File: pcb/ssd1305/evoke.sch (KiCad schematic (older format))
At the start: 17 parts, among them U1 STM32F103C8Tx

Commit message: Fix bug with pins being wrong on connector, and add USART header
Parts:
- added J1: Conn_01x03_Male, Connector_PinHeader_2.54mm:PinHeader_1x03_P2.54mm_Vertical, symbol Connector:Conn_01x03_Male
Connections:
- net +3V3: now also LCD_CONN1.21 (Pin_21); no longer LCD_CONN1.20 (Pin_20)
- net GND: now also LCD_CONN1.20 (Pin_20), J1.3 (Pin_3); no longer LCD_CONN1.21 (Pin_21)
- net USART1_TX: now reaches U1.30 (PA9)
- net USART1_TX: now also J1.1 (Pin_1)
- net USART1_RX: now reaches U1.31 (PA10)
- net USART1_RX: now also J1.2 (Pin_2)
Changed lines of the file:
@@
-	1    0    0    -1
-$EndComp
-$Comp
-L evoke-rescue:GND-power #PWR0102
-U 1 1 5EAB6769
-P 3600 5250
-F 0 "#PWR0102" H 3600 5000 50  0001 C CNN
-F 1 "GND" H 3605 5077 50  0000 C CNN
-F 2 "" H 3600 5250 50  0001 C CNN
-F 3 "" H 3600 5250 50  0001 C CNN
-	1    3600 5250
 	1    0    0    -1
 $EndComp
@@
 L evoke-rescue:GND-power #PWR0103
 U 1 1 5EABAA37
-P 3400 5250
-F 0 "#PWR0103" H 3400 5000 50  0001 C CNN
-F 1 "GND" H 3405 5077 50  0000 C CNN
-F 2 "" H 3400 5250 50  0001 C CNN
-F 3 "" H 3400 5250 50  0001 C CNN
-	1    3400 5250
-	1    0    0    -1
-$EndComp
-$Comp
-L evoke-rescue:+3V3-power #PWR0104
-U 1 1 5EABC207
 P 3500 5250
-F 0 "#PWR0104" H 3500 5100 50  0001 C CNN
-F 1 "+3V3" H 3515 5423 50  0000 C CNN
+F 0 "#PWR0103" H 3500 5000 50  0001 C CNN
+F 1 "GND" H 3505 5077 50  0000 C CNN
 F 2 "" H 3500 5250 50  0001 C CNN
 F 3 "" H 3500 5250 50  0001 C CNN
@@
 Wire Wire Line
 	9850 2150 10000 2150
+Wire Wire Line
+	3400 5250 3500 5250
+Connection ~ 3500 5250
+Wire Wire Line
+	4200 5250 3600 5250
+Connection ~ 4200 5250
+Wire Wire Line
+	6350 3600 6550 3600
+Wire Wire Line
+	6350 3700 6550 3700
+Text GLabel 6550 3600 2    50   Input ~ 0
+USART1_TX
+Text GLabel 6550 3700 2    50   Input ~ 0
+USART1_RX
+$Comp
+L Connector:Conn_01x03_Male J1
+U 1 1 5ED86F10
+P 5550 5700
+F 0 "J1" H 5658 5981 50  0000 C CNN
+F 1 "Conn_01x03_Male" H 5658 5890 50  0000 C CNN
+F 2 "Connector_PinHeader_2.54mm:PinHeader_1x03_P2.54mm_Vertical" H 5550 5700 50  0001 C CNN
+F 3 "~" H 5550 5700 50  0001 C CNN
+	1    5550 5700
+	1    0    0    -1
+$EndComp
+Wire Wire Line
+	5750 5600 6050 5600
+Wire Wire Line
+	5750 5700 6050 5700
+Wire Wire Line
+	5750 5800 6050 5800
+$Comp
+L power:GND #PWR0102
+U 1 1 5ED93166
+P 6050 5800
+F 0 "#PWR0102" H 6050 5550 50  0001 C CNN
+F 1 "GND" H 6055 5627 50  0000 C CNN
+F 2 "" H 6050 5800 50  0001 C CNN
+F 3 "" H 6050 5800 50  0001 C CNN
+	1    6050 5800
+	1    0    0    -1
+$EndComp
+Text GLabel 6050 5600 2    50   Input ~ 0
+USART1_TX
+Text GLabel 6050 5700 2    50   Input ~ 0
+USART1_RX
 $EndSCHEMATC

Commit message: Addition of additional components as per jack wan's schematic example
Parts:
- removed C10: 100nF, Capacitor_SMD:C_0805_2012Metric, symbol evoke-rescue:C-Device
- added C10, C12: 100nF, Capacitor_SMD:C_0805_2012Metric, symbol Device:C
- added C11: 10uF, Capacitor_Tantalum_SMD:CP_EIA-3216-18_Kemet-A, symbol Device:CP
- added C13: 4.7uF, Capacitor_Tantalum_SMD:CP_EIA-3216-18_Kemet-A, symbol evoke-rescue:CP-Device
- C1: value 10uF -> 4.7uF; LCSC C7171 -> (none)
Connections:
- net +3V3: now also C12.1, C13.1
- net GND: now also C10.2, C11.2, C12.2, C13.2
- net VCC: now also C10.1, C11.1
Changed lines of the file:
@@
 P 1800 5900
 F 0 "C1" H 1918 5946 50  0000 L CNN
-F 1 "10uF" H 1918 5855 50  0000 L CNN
+F 1 "4.7uF" H 1918 5855 50  0000 L CNN
 F 2 "Capacitor_Tantalum_SMD:CP_EIA-3216-18_Kemet-A" H 1838 5750 50  0001 C CNN
 F 3 "~" H 1800 5900 50  0001 C CNN
-F 4 " C7171" H 1800 5900 50  0001 C CNN "LCSC"
+F 4 " " H 1800 5900 50  0001 C CNN "LCSC"
 	1    1800 5900
 	1    0    0    -1
@@
 	1    0    0    -1
 $EndComp
-$Comp
-L evoke-rescue:C-Device C10
-U 1 1 5EA8CE78
-P 2150 5900
-F 0 "C10" H 2265 5946 50  0000 L CNN
-F 1 "100nF" H 2265 5855 50  0000 L CNN
-F 2 "Capacitor_SMD:C_0805_2012Metric" H 2188 5750 50  0001 C CNN
-F 3 "~" H 2150 5900 50  0001 C CNN
-F 4 "C49678" H 2150 5900 50  0001 C CNN "LCSC"
-	1    2150 5900
-	1    0    0    -1
-$EndComp
-Wire Wire Line
-	2150 6050 1800 6050
-Connection ~ 1800 6050
-Wire Wire Line
-	2150 5750 1800 5750
-Connection ~ 1800 5750
 Wire Wire Line
 	6350 4000 6750 4000
@@
 Text GLabel 6050 5700 2    50   Input ~ 0
 USART1_RX
+$Comp
+L Device:C C10
+U 1 1 5ED7135E
+P 1950 6650
+F 0 "C10" H 1750 6700 50  0000 L CNN
+F 1 "100nF" H 1650 6600 50  0000 L CNN
+F 2 "Capacitor_SMD:C_0805_2012Metric" H 1988 6500 50  0001 C CNN
+F 3 "~" H 1950 6650 50  0001 C CNN
+	1    1950 6650
+	1    0    0    -1
+$EndComp
+$Comp
+L Device:CP C11
+U 1 1 5ED73E93
+P 2250 6650
+F 0 "C11" H 2368 6696 50  0000 L CNN
+F 1 "10uF" H 2368 6605 50  0000 L CNN
+F 2 "Capacitor_Tantalum_SMD:CP_EIA-3216-18_Kemet-A" H 2288 6500 50  0001 C CNN
+F 3 "~" H 2250 6650 50  0001 C CNN
+	1    2250 6650
+	1    0    0    -1
+$EndComp
+Wire Wire Line
+	1950 6800 2100 6800
+Wire Wire Line
+	1950 6500 2100 6500
+$Comp
+L power:GND #PWR0104
+U 1 1 5ED7C439
+P 2100 6800
+F 0 "#PWR0104" H 2100 6550 50  0001 C CNN
+F 1 "GND" H 2105 6627 50  0000 C CNN
+F 2 "" H 2100 6800 50  0001 C CNN
+F 3 "" H 2100 6800 50  0001 C CNN
+	1    2100 6800
+	1    0    0    -1
+$EndComp
+Connection ~ 2100 6800
+Wire Wire Line
+	2100 6800 2250 6800
+Text GLabel 2100 6400 1    50   Input ~ 0
+VCC
+Wire Wire Line
+	2100 6400 2100 6500
+Connection ~ 2100 6500
+Wire Wire Line
+	2100 6500 2250 6500
+$Comp
+L evoke-rescue:CP-Device C13
+U 1 1 5ED88180
+P 3250 6600
+F 0 "C13" H 3368 6646 50  0000 L CNN
+F 1 "4.7uF" H 3368 6555 50  0000 L CNN
+F 2 "Capacitor_Tantalum_SMD:CP_EIA-3216-18_Kemet-A" H 3288 6450 50  0001 C CNN
+F 3 "~" H 3250 6600 50  0001 C CNN
+F 4 " " H 3250 6600 50  0001 C CNN "LCSC"
+	1    3250 6600
+	1    0    0    -1
+$EndComp
+$Comp
+L Device:C C12
+U 1 1 5ED88A1A
+P 3000 6600
+F 0 "C12" H 2800 6650 50  0000 L CNN
+F 1 "100nF" H 2700 6550 50  0000 L CNN
+F 2 "Capacitor_SMD:C_0805_2012Metric" H 3038 6450 50  0001 C CNN
+F 3 "~" H 3000 6600 50  0001 C CNN
+	1    3000 6600
+	1    0    0    -1
+$EndComp
+Wire Wire Line
+	3000 6750 3100 6750
+Wire Wire Line
+	3250 6450 3100 6450
+$Comp
+L evoke-rescue:+3V3-power #PWR0114
+U 1 1 5ED91A37
+P 3100 6450
+F 0 "#PWR0114" H 3100 6300 50  0001 C CNN
+F 1 "+3V3" H 3115 6623 50  0000 C CNN
+F 2 "" H 3100 6450 50  0001 C CNN
+F 3 "" H 3100 6450 50  0001 C CNN
+	1    3100 6450
+	1    0    0    -1
+$EndComp
+Connection ~ 3100 6450
+Wire Wire Line
+	3100 6450 3000 6450
+$Comp
+L power:GND #PWR0115
+U 1 1 5ED921BC
+P 3100 6750
+F 0 "#PWR0115" H 3100 6500 50  0001 C CNN
+F 1 "GND" H 3105 6577 50  0000 C CNN
+F 2 "" H 3100 6750 50  0001 C CNN
+F 3 "" H 3100 6750 50  0001 C CNN
+	1    3100 6750
+	1    0    0    -1
+$EndComp
+Connection ~ 3100 6750
+Wire Wire Line
+	3100 6750 3250 6750
 $EndSCHEMATC

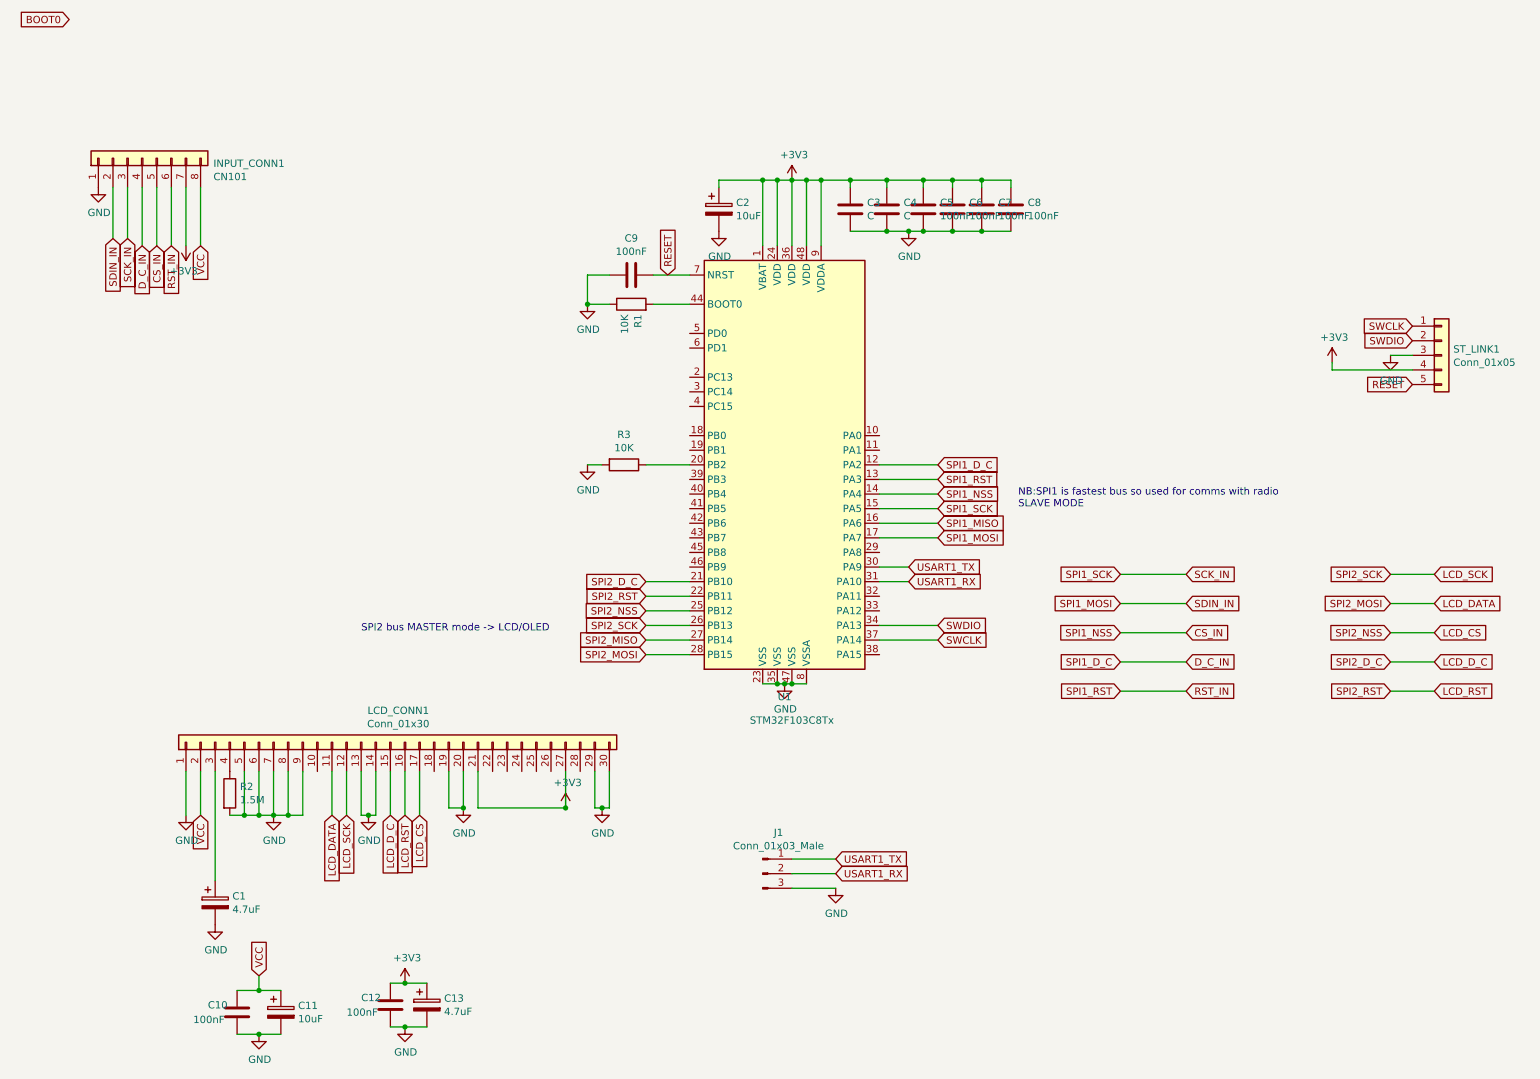
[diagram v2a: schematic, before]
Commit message: Put next revision into manufacture - hopefully ready to go, now with test points!
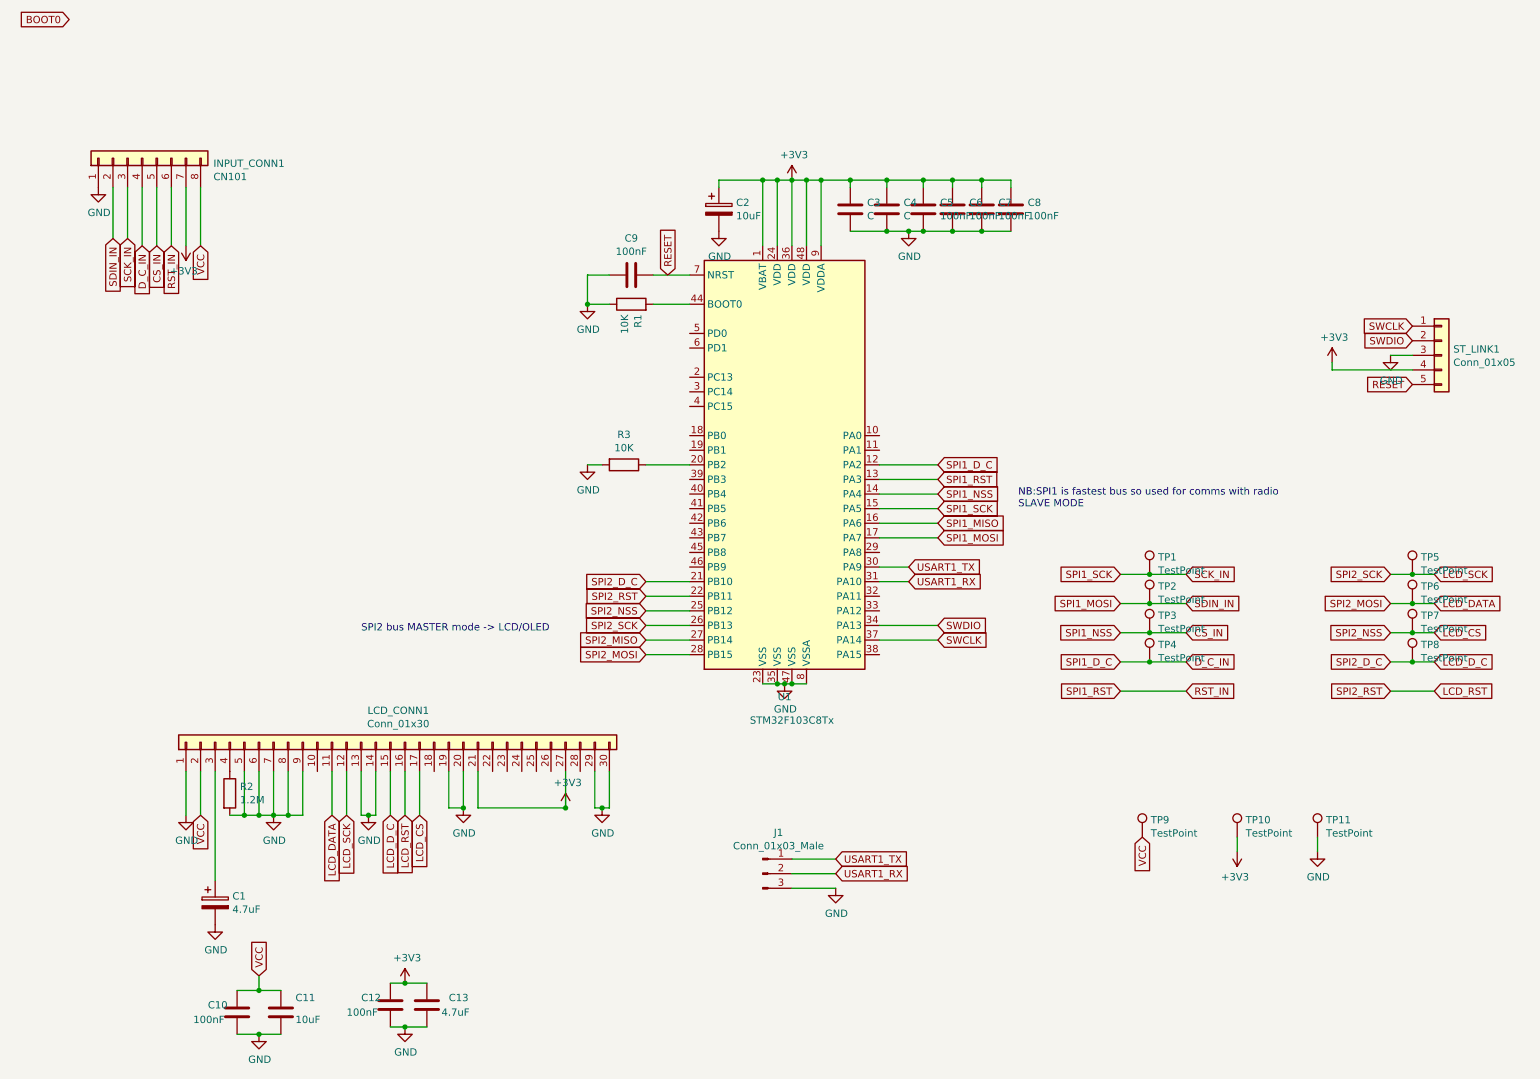
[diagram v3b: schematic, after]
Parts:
- removed C11: 10uF, Capacitor_Tantalum_SMD:CP_EIA-3216-18_Kemet-A, symbol Device:CP
- removed C13: 4.7uF, Capacitor_Tantalum_SMD:CP_EIA-3216-18_Kemet-A, symbol evoke-rescue:CP-Device
- added C11: 10uF, Capacitor_SMD:C_0805_2012Metric, symbol Device:C
- added C13: 4.7uF, Capacitor_SMD:C_0805_2012Metric, symbol Device:C
- added TP1, TP10, TP11, TP2, TP3, TP4, TP5, TP6, TP7, TP8, TP9: TestPoint, TestPoint:TestPoint_Pad_D1.0mm, symbol Connector:TestPoint
- C1: LCSC (none) -> C161817
- C10, C12: LCSC (none) -> C49678
- R2: value 1.5M -> 1.2M; LCSC C26110 -> C17380
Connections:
- net +3V3: now also C13.1, TP10.1
- net CS_IN: now also TP3.1
- net D_C_IN: now also TP4.1
- net GND: now also C11.2, C13.2, TP11.1
- net LCD_CS: now also TP7.1
- net LCD_DATA: now also TP6.1
- net LCD_D_C: now also TP8.1
- net LCD_SCK: now also TP5.1
- net SCK_IN: now also TP1.1
- net SDIN_IN: now also TP2.1
- net VCC: now also C11.1, TP9.1
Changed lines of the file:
@@
 $EndComp
 Wire Wire Line
-	9850 3650 10150 3650
+	9850 3650 10000 3650
 Text GLabel 10150 3650 2    50   Input ~ 0
 LCD_SCK
@@
 SPI2_SCK
 Wire Wire Line
-	9850 3850 10150 3850
-Wire Wire Line
-	10150 4050 9850 4050
-Wire Wire Line
-	9850 4250 10150 4250
+	9850 3850 10000 3850
+Wire Wire Line
+	10150 4050 10000 4050
+Wire Wire Line
+	9850 4250 10000 4250
 Text GLabel 9850 4050 0    50   Input ~ 0
 SPI2_NSS
@@
 SPI2_RST
 Wire Wire Line
-	8000 3650 8450 3650
-Wire Wire Line
-	8000 3850 8450 3850
-Wire Wire Line
-	8000 4050 8450 4050
-Wire Wire Line
-	8000 4250 8450 4250
+	8000 3650 8200 3650
+Wire Wire Line
+	8000 3850 8200 3850
+Wire Wire Line
+	8000 4050 8200 4050
+Wire Wire Line
+	8000 4250 8200 4250
 Wire Wire Line
 	8000 4450 8450 4450
@@
 P 1900 5150
 F 0 "R2" H 1970 5196 50  0000 L CNN
-F 1 "1.5M" H 1970 5105 50  0000 L CNN
+F 1 "1.2M" H 1970 5105 50  0000 L CNN
 F 2 "Resistor_SMD:R_0805_2012Metric" V 1830 5150 50  0001 C CNN
 F 3 "~" H 1900 5150 50  0001 C CNN
-F 4 "C26110" H 1900 5150 50  0001 C CNN "LCSC"
+F 4 "C17380" H 1900 5150 50  0001 C CNN "LCSC"
 	1    1900 5150
 	1    0    0    -1
@@
 F 2 "Capacitor_Tantalum_SMD:CP_EIA-3216-18_Kemet-A" H 1838 5750 50  0001 C CNN
 F 3 "~" H 1800 5900 50  0001 C CNN
-F 4 " " H 1800 5900 50  0001 C CNN "LCSC"
+F 4 "C161817" H 1800 5900 50  0001 C CNN "LCSC"
 	1    1800 5900
 	1    0    0    -1
@@
 F 2 "Capacitor_SMD:C_0805_2012Metric" H 1988 6500 50  0001 C CNN
 F 3 "~" H 1950 6650 50  0001 C CNN
+F 4 "C49678" H 1950 6650 50  0001 C CNN "LCSC"
 	1    1950 6650
-	1    0    0    -1
-$EndComp
-$Comp
-L Device:CP C11
-U 1 1 5ED73E93
-P 2250 6650
-F 0 "C11" H 2368 6696 50  0000 L CNN
-F 1 "10uF" H 2368 6605 50  0000 L CNN
-F 2 "Capacitor_Tantalum_SMD:CP_EIA-3216-18_Kemet-A" H 2288 6500 50  0001 C CNN
-F 3 "~" H 2250 6650 50  0001 C CNN
-	1    2250 6650
 	1    0    0    -1
 $EndComp
@@
 	2100 6500 2250 6500
 $Comp
-L evoke-rescue:CP-Device C13
-U 1 1 5ED88180
-P 3250 6600
-F 0 "C13" H 3368 6646 50  0000 L CNN
-F 1 "4.7uF" H 3368 6555 50  0000 L CNN
-F 2 "Capacitor_Tantalum_SMD:CP_EIA-3216-18_Kemet-A" H 3288 6450 50  0001 C CNN
-F 3 "~" H 3250 6600 50  0001 C CNN
-F 4 " " H 3250 6600 50  0001 C CNN "LCSC"
-	1    3250 6600
-	1    0    0    -1
-$EndComp
-$Comp
 L Device:C C12
 U 1 1 5ED88A1A
@@
 F 2 "Capacitor_SMD:C_0805_2012Metric" H 3038 6450 50  0001 C CNN
 F 3 "~" H 3000 6600 50  0001 C CNN
+F 4 "C49678" H 3000 6600 50  0001 C CNN "LCSC"
 	1    3000 6600
 	1    0    0    -1
@@
 Wire Wire Line
 	3100 6750 3250 6750
+$Comp
+L Device:C C13
+U 1 1 5ED72B7A
+P 3250 6600
+F 0 "C13" H 3400 6650 50  0000 L CNN
+F 1 "4.7uF" H 3350 6550 50  0000 L CNN
+F 2 "Capacitor_SMD:C_0805_2012Metric" H 3288 6450 50  0001 C CNN
+F 3 "~" H 3250 6600 50  0001 C CNN
+F 4 "C1779" H 3250 6600 50  0001 C CNN "LCSC"
+	1    3250 6600
+	1    0    0    -1
+$EndComp
+$Comp
+L Device:C C11
+U 1 1 5ED738B1
+P 2250 6650
+F 0 "C11" H 2350 6750 50  0000 L CNN
+F 1 "10uF" H 2350 6600 50  0000 L CNN
+F 2 "Capacitor_SMD:C_0805_2012Metric" H 2288 6500 50  0001 C CNN
+F 3 "~" H 2250 6650 50  0001 C CNN
+F 4 "C15850" H 2250 6650 50  0001 C CNN "LCSC"
+	1    2250 6650
+	1    0    0    -1
+$EndComp
+$Comp
+L Connector:TestPoint TP1
+U 1 1 5ED9606D
+P 8200 3650
+F 0 "TP1" H 8258 3768 50  0000 L CNN
+F 1 "TestPoint" H 8258 3677 50  0000 L CNN
+F 2 "TestPoint:TestPoint_Pad_D1.0mm" H 8400 3650 50  0001 C CNN
+F 3 "~" H 8400 3650 50  0001 C CNN
+	1    8200 3650
+	1    0    0    -1
+$EndComp
+Connection ~ 8200 3650
+Wire Wire Line
+	8200 3650 8450 3650
+$Comp
+L Connector:TestPoint TP2
+U 1 1 5ED9662E
+P 8200 3850
+F 0 "TP2" H 8258 3968 50  0000 L CNN
+F 1 "TestPoint" H 8258 3877 50  0000 L CNN
+F 2 "TestPoint:TestPoint_Pad_D1.0mm" H 8400 3850 50  0001 C CNN
+F 3 "~" H 8400 3850 50  0001 C CNN
+	1    8200 3850
+	1    0    0    -1
+$EndComp
+Connection ~ 8200 3850
+Wire Wire Line
+	8200 3850 8450 3850
+$Comp
+L Connector:TestPoint TP3
+U 1 1 5ED969D3
+P 8200 4050
+F 0 "TP3" H 8258 4168 50  0000 L CNN
+F 1 "TestPoint" H 8258 4077 50  0000 L CNN
+F 2 "TestPoint:TestPoint_Pad_D1.0mm" H 8400 4050 50  0001 C CNN
+F 3 "~" H 8400 4050 50  0001 C CNN
+	1    8200 4050
+	1    0    0    -1
+$EndComp
+Connection ~ 8200 4050
+Wire Wire Line
+	8200 4050 8450 4050
+$Comp
+L Connector:TestPoint TP4
+U 1 1 5ED96D81
+P 8200 4250
+F 0 "TP4" H 8258 4368 50  0000 L CNN
+F 1 "TestPoint" H 8258 4277 50  0000 L CNN
+F 2 "TestPoint:TestPoint_Pad_D1.0mm" H 8400 4250 50  0001 C CNN
+F 3 "~" H 8400 4250 50  0001 C CNN
+	1    8200 4250
+	1    0    0    -1
+$EndComp
+Connection ~ 8200 4250
+Wire Wire Line
+	8200 4250 8450 4250
+$Comp
+L Connector:TestPoint TP5
+U 1 1 5ED97130
+P 10000 3650
+F 0 "TP5" H 10058 3768 50  0000 L CNN
+F 1 "TestPoint" H 10058 3677 50  0000 L CNN
+F 2 "TestPoint:TestPoint_Pad_D1.0mm" H 10200 3650 50  0001 C CNN
+F 3 "~" H 10200 3650 50  0001 C CNN
+	1    10000 3650
+	1    0    0    -1
+$EndComp
+Connection ~ 10000 3650
+Wire Wire Line
+	10000 3650 10150 3650
+$Comp
+L Connector:TestPoint TP6
+U 1 1 5ED97530
+P 10000 3850
+F 0 "TP6" H 10058 3968 50  0000 L CNN
+F 1 "TestPoint" H 10058 3877 50  0000 L CNN
+F 2 "TestPoint:TestPoint_Pad_D1.0mm" H 10200 3850 50  0001 C CNN
+F 3 "~" H 10200 3850 50  0001 C CNN
+	1    10000 3850
+	1    0    0    -1
+$EndComp
+Connection ~ 10000 3850
+Wire Wire Line
+	10000 3850 10150 3850
+$Comp
+L Connector:TestPoint TP7
+U 1 1 5ED98084
+P 10000 4050
+F 0 "TP7" H 10058 4168 50  0000 L CNN
+F 1 "TestPoint" H 10058 4077 50  0000 L CNN
+F 2 "TestPoint:TestPoint_Pad_D1.0mm" H 10200 4050 50  0001 C CNN
+F 3 "~" H 10200 4050 50  0001 C CNN
+	1    10000 4050
+	1    0    0    -1
+$EndComp
+Connection ~ 10000 4050
+Wire Wire Line
+	10000 4050 9850 4050
+$Comp
+L Connector:TestPoint TP8
+U 1 1 5ED9844C
+P 10000 4250
+F 0 "TP8" H 10058 4368 50  0000 L CNN
+F 1 "TestPoint" H 10058 4277 50  0000 L CNN
+F 2 "TestPoint:TestPoint_Pad_D1.0mm" H 10200 4250 50  0001 C CNN
+F 3 "~" H 10200 4250 50  0001 C CNN
+	1    10000 4250
+	1    0    0    -1
+$EndComp
+Connection ~ 10000 4250
+Wire Wire Line
+	10000 4250 10150 4250
+$Comp
+L Connector:TestPoint TP9
+U 1 1 5EDB4575
+P 8150 5450
+F 0 "TP9" H 8208 5568 50  0000 L CNN
+F 1 "TestPoint" H 8208 5477 50  0000 L CNN
+F 2 "TestPoint:TestPoint_Pad_D1.0mm" H 8350 5450 50  0001 C CNN
+F 3 "~" H 8350 5450 50  0001 C CNN
+	1    8150 5450
+	1    0    0    -1
+$EndComp
+$Comp
+L Connector:TestPoint TP10
+U 1 1 5EDB49DE
+P 8800 5450
+F 0 "TP10" H 8858 5568 50  0000 L CNN
+F 1 "TestPoint" H 8858 5477 50  0000 L CNN
+F 2 "TestPoint:TestPoint_Pad_D1.0mm" H 9000 5450 50  0001 C CNN
+F 3 "~" H 9000 5450 50  0001 C CNN
+	1    8800 5450
+	1    0    0    -1
+$EndComp
+$Comp
+L Connector:TestPoint TP11
+U 1 1 5EDB4E21
+P 9350 5450
+F 0 "TP11" H 9408 5568 50  0000 L CNN
+F 1 "TestPoint" H 9408 5477 50  0000 L CNN
+F 2 "TestPoint:TestPoint_Pad_D1.0mm" H 9550 5450 50  0001 C CNN
+F 3 "~" H 9550 5450 50  0001 C CNN
+	1    9350 5450
+	1    0    0    -1
+$EndComp
+Text GLabel 8150 5450 3    50   Input ~ 0
+VCC
+$Comp
+L evoke-rescue:+3V3-power #PWR0122
+U 1 1 5EDCAEA9
+P 8800 5550
+F 0 "#PWR0122" H 8800 5400 50  0001 C CNN
+F 1 "+3V3" H 8815 5723 50  0000 C CNN
+F 2 "" H 8800 5550 50  0001 C CNN
+F 3 "" H 8800 5550 50  0001 C CNN
+	1    8800 5550
+	-1   0    0    1
+$EndComp
+$Comp
+L evoke-rescue:GND-power #PWR0123
+U 1 1 5EDCB476
+P 9350 5550
+F 0 "#PWR0123" H 9350 5300 50  0001 C CNN
+F 1 "GND" H 9355 5377 50  0000 C CNN
+F 2 "" H 9350 5550 50  0001 C CNN
+F 3 "" H 9350 5550 50  0001 C CNN
+	1    9350 5550
+	1    0    0    -1
+$EndComp
+Wire Wire Line
+	9350 5550 9350 5450
+Wire Wire Line
+	8800 5550 8800 5450
 $EndSCHEMATC
